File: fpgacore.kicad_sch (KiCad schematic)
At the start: 10 parts, among them U6 XC7A35T-FGG484

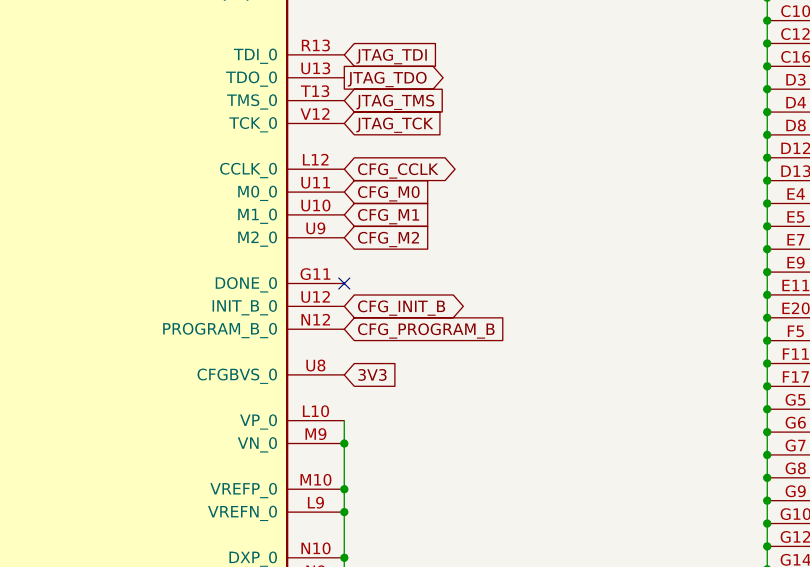
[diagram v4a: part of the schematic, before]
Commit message: Routing in progress: In3 power pours, DONE LED, DRC cleanup
- Add CFG_DONE 330R pull-up (R52) and DONE LED (D7, R53) per UG470
- Redraw In3.Cu pours to sit under their U6 balls (1V0 core, 1V8 strip,
  MGTAVCC, MGTAVTT); trim 5V_LC strip to y=50; zone clearance 0.2mm
- Remove 3V3/5V_LC traces from In4.Cu GND plane
- Custom rules: U6 BGA escape, solid GND on regulators/tight caps,
  1-spoke thermals on J4 and C22
- Fix clearance violations, remove dangling vias and stubs
- Remaining: GND pours split on In1.Cu/B.Cu by signal traces on In1.Cu
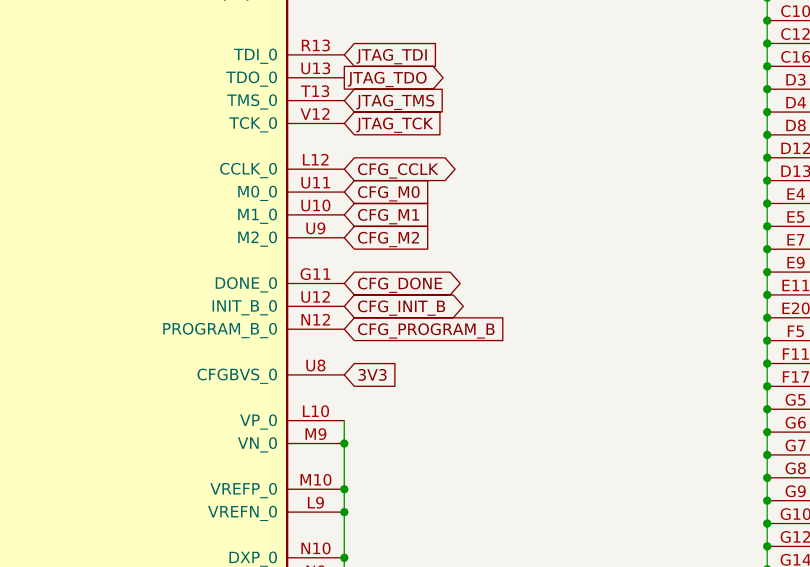
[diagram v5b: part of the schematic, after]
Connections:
- net CFG_DONE: now reaches U6.G11 (DONE_0)
- no-connect marks 212 -> 211
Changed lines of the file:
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@@
 	)
 	(no_connect
-		(at 140.97 203.2)
-	)
-	(no_connect
 		(at 453.39 74.93)
 	)
@@
 			)
 		)
+	)
+	(global_label "CFG_DONE"
+		(shape bidirectional)
+		(at 140.97 203.2 0)
+		(fields_autoplaced yes)
+		(effects
+			(font
+				(size 1.27 1.27)
+			)
+			(justify left)
+		)
+		(property "Intersheetrefs" "${INTERSHEET_REFS}"
+			(at 140.97 203.2 0)
+			(hide yes)
+			(show_name no)
+			(do_not_autoplace no)
+			(effects
+				(font
+					(size 1.27 1.27)
+				)
+				(justify left)
+			)
+		)
